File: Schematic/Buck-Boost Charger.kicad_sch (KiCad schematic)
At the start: 79 parts, among them U13 BQ25756RRVR

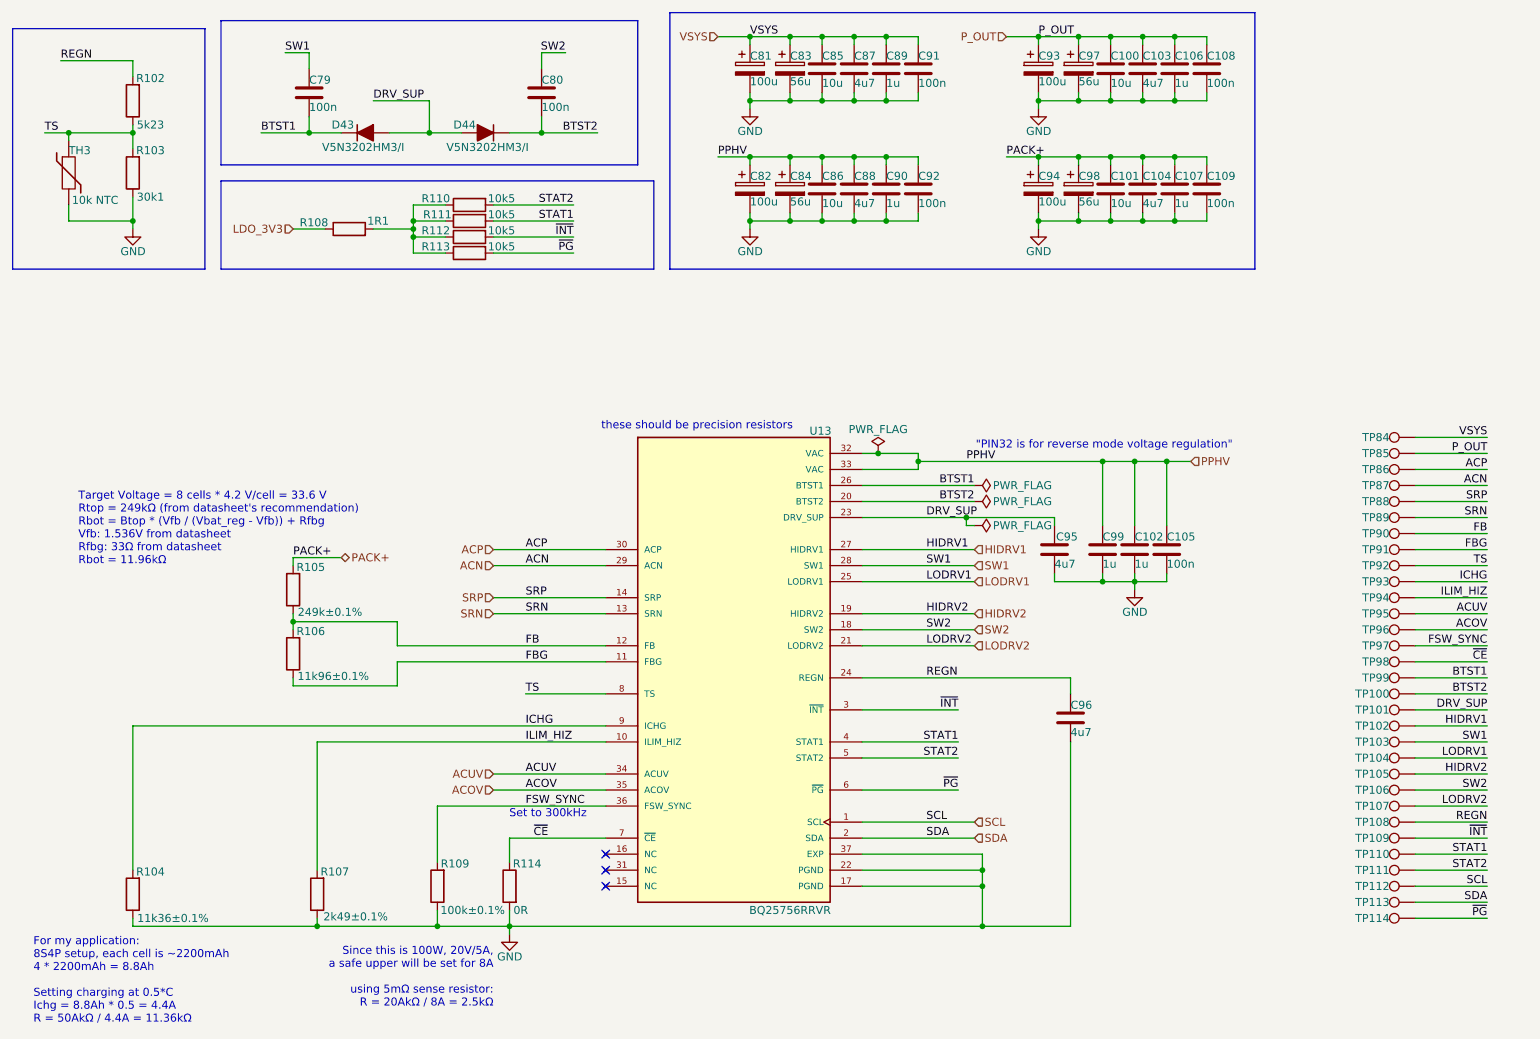
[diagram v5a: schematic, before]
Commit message: updated fuel guage
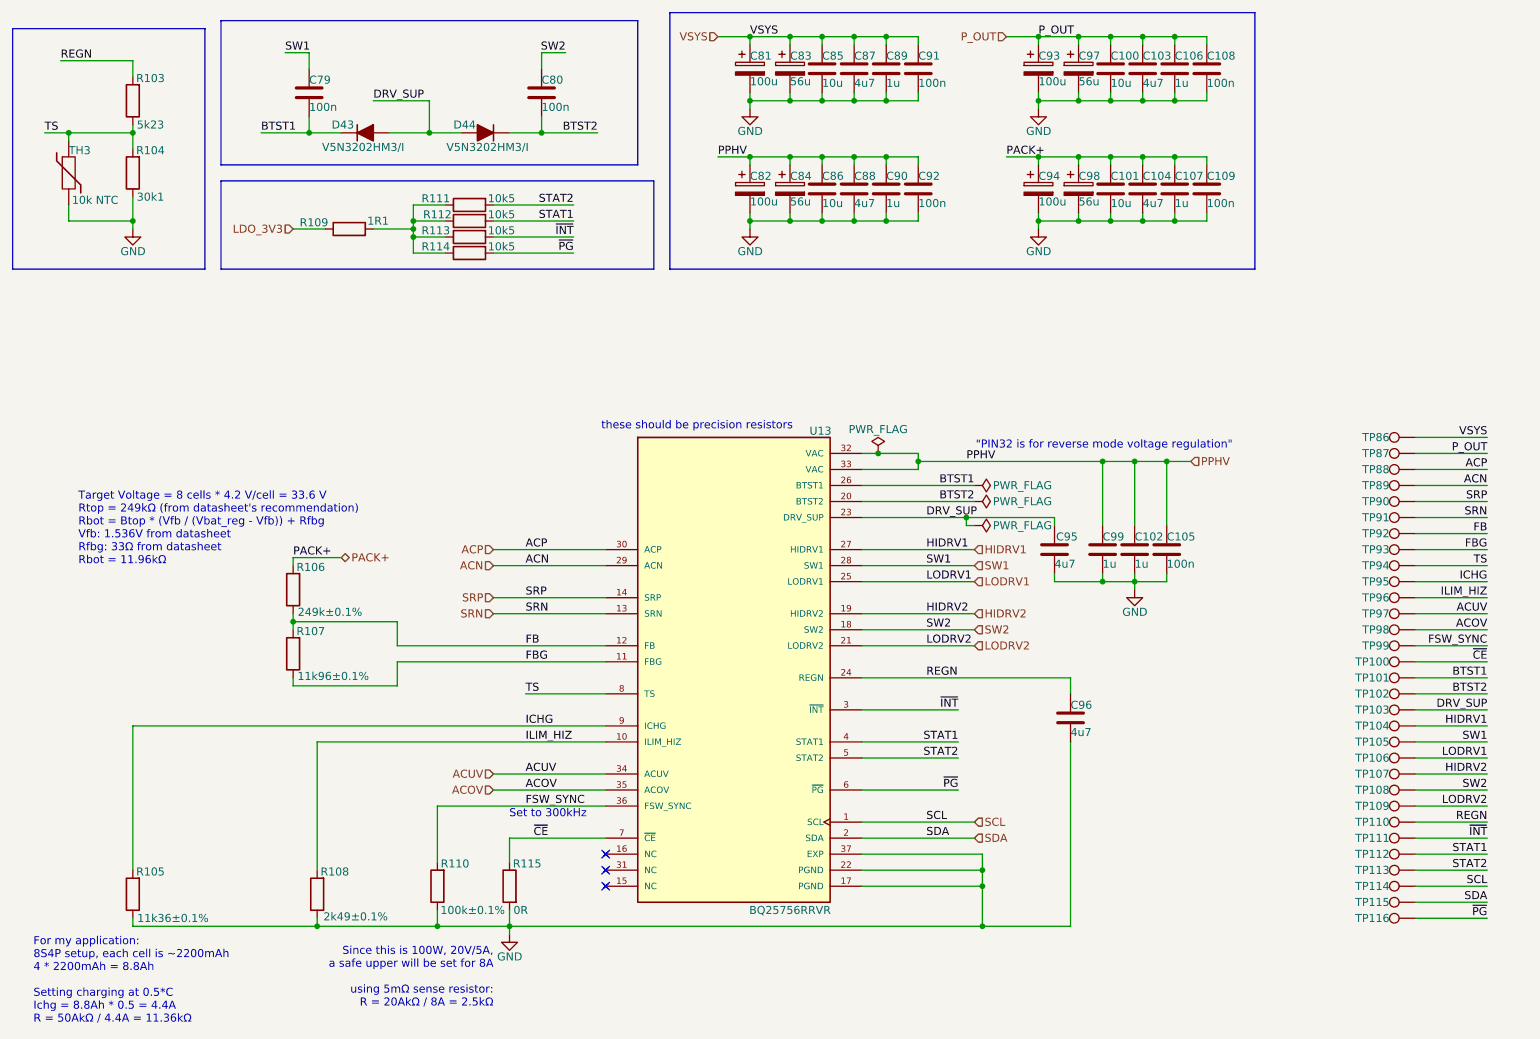
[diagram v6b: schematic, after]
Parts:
- renumbered R102 to R103, R103 to R104, R104 to R105, R105 to R106, R106 to R107, R107 to R108, R108 to R109, R109 to R110, R110 to R111, R111 to R112, R112 to R113, R113 to R114, R114 to R115, TP98 to TP100, TP99 to TP101, TP100 to TP102, TP101 to TP103, TP102 to TP104, TP103 to TP105, TP104 to TP106, TP105 to TP107, TP106 to TP108, TP107 to TP109, TP108 to TP110, TP109 to TP111, TP110 to TP112, TP111 to TP113, TP112 to TP114, TP113 to TP115, TP114 to TP116, TP84 to TP86, TP85 to TP87, TP86 to TP88, TP87 to TP89, TP88 to TP90, TP89 to TP91, TP90 to TP92, TP91 to TP93, TP92 to TP94, TP93 to TP95, TP94 to TP96, TP95 to TP97, TP96 to TP98, TP97 to TP99

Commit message: Added MCU
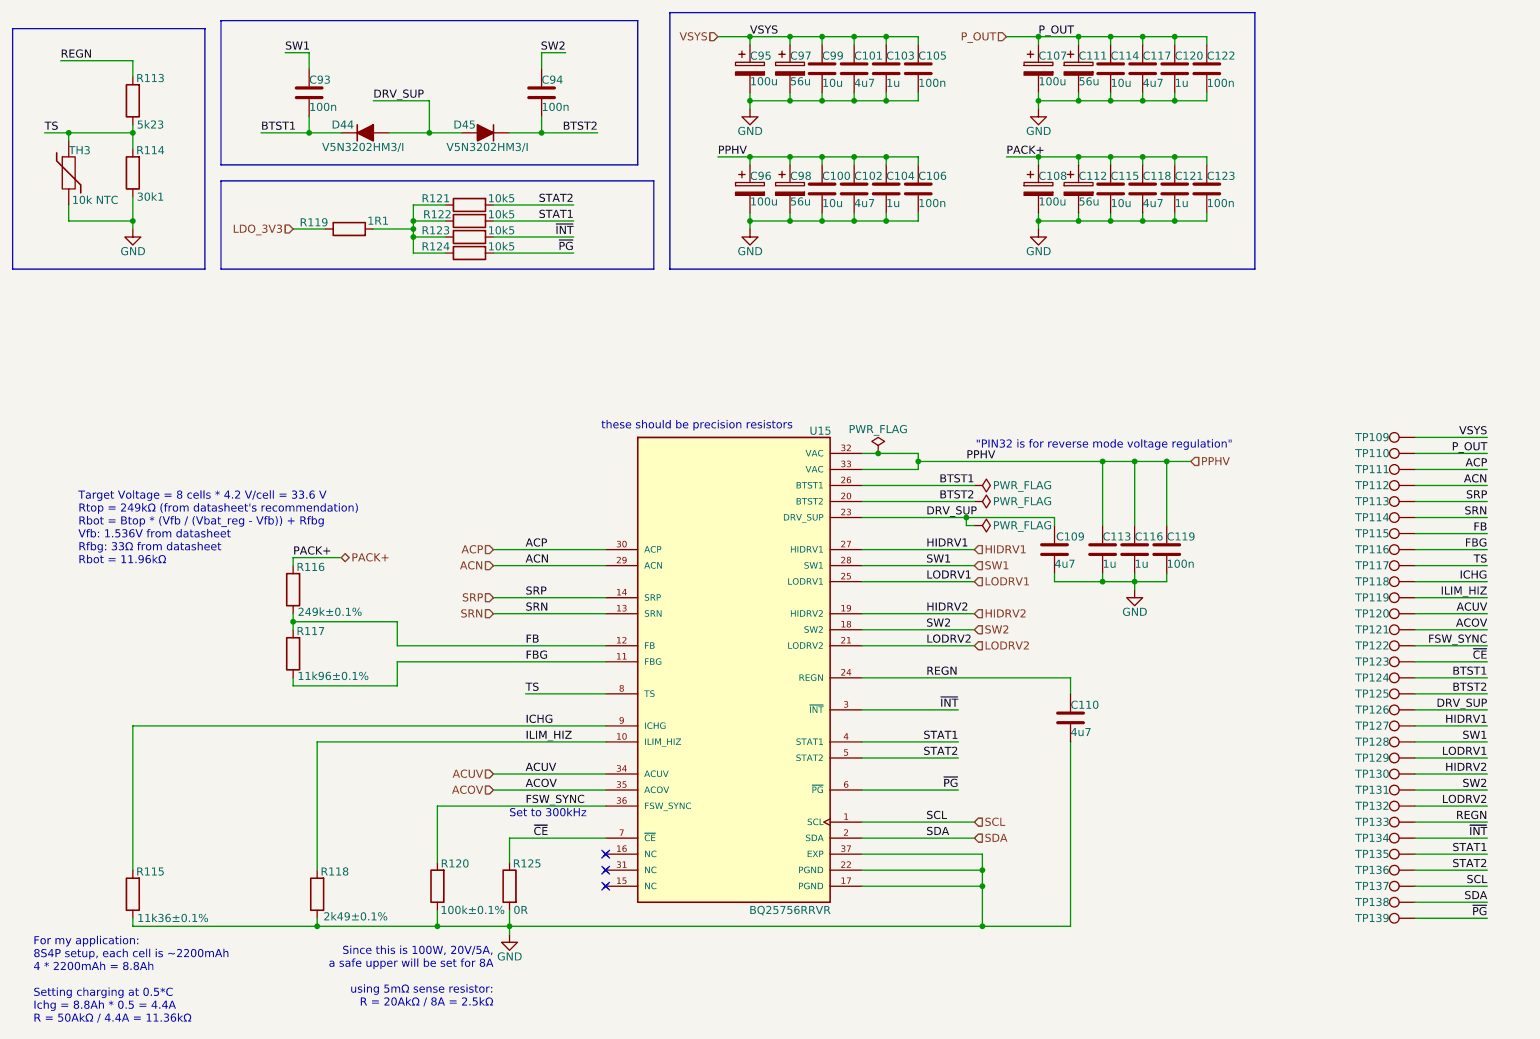
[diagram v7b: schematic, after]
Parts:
- renumbered C86 to C100, C87 to C101, C88 to C102, C89 to C103, C90 to C104, C91 to C105, C92 to C106, C93 to C107, C94 to C108, C95 to C109, C96 to C110, C97 to C111, C98 to C112, C99 to C113, C100 to C114, C101 to C115, C102 to C116, C103 to C117, C104 to C118, C105 to C119, C106 to C120, C107 to C121, C108 to C122, C109 to C123, C79 to C93, C80 to C94, C81 to C95, C82 to C96, C83 to C97, C84 to C98, C85 to C99, D43 to D44, D44 to D45, R103 to R113, R104 to R114, R105 to R115, R106 to R116, R107 to R117, R108 to R118, R109 to R119, R110 to R120, R111 to R121, R112 to R122, R113 to R123, R114 to R124, R115 to R125, TP86 to TP109, TP87 to TP110, TP88 to TP111, TP89 to TP112, TP90 to TP113, TP91 to TP114, TP92 to TP115, TP93 to TP116, TP94 to TP117, TP95 to TP118, TP96 to TP119, TP97 to TP120, TP98 to TP121, TP99 to TP122, TP100 to TP123, TP101 to TP124, TP102 to TP125, TP103 to TP126, TP104 to TP127, TP105 to TP128, TP106 to TP129, TP107 to TP130, TP108 to TP131, TP109 to TP132, TP110 to TP133, TP111 to TP134, TP112 to TP135, TP113 to TP136, TP114 to TP137, TP115 to TP138, TP116 to TP139, U13 to U15

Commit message: Started to work on the BOM
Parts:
- removed C100, C114: 10u, symbol Device:C
- removed C101: 4u7, symbol Device:C
- removed C104, C120: 1u, symbol Device:C
- removed C107, C108, C96: 100u, symbol Device:C_Polarized
- removed C122: 100n, symbol Device:C
- removed C97, C98: 56u, symbol Device:C_Polarized
- removed D44, D45: V5N3202HM3/I, symbol Device:D_Filled
- added C109, C110, C112, C113, C90, C91, C92, C93, C94: 56u, AHA0810560M040R:CAPAE830X1100M, symbol Device:C_Polarized
- added C115, C96, C97: 10u, Capacitor_SMD:C_1206_3216Metric_Pad1.33x1.80mm_HandSolder, symbol Device:C
- added C119: 1u, Capacitor_SMD:C_1206_3216Metric_Pad1.33x1.80mm_HandSolder, symbol Device:C
- added C121: 100n, Capacitor_SMD:C_1206_3216Metric_Pad1.33x1.80mm_HandSolder, symbol Device:C
- added C98: 4u7, Capacitor_SMD:C_1206_3216Metric_Pad1.33x1.80mm_HandSolder, symbol Device:C
- added D41, D42: V5N3202HM3/I, V5N3202HM3-I:DFN33A_VIS, symbol V5N3202HM3-I:V5N3202HM3_I
- C100: renamed from C109; footprint (none) -> Capacitor_SMD:C_1206_3216Metric_Pad1.33x1.80mm_HandSolder; Link (none) -> https://mou.sr/45jYGQI; Manufacturer Part Number (none) -> CL31B475KBHNFNE; Price per Unit (none) -> 0.27; Supplier (none) -> Mouser; Supplier Part Number (none) -> 187-CL31B475KBHNFNE
- C101: renamed from C110; footprint (none) -> Capacitor_SMD:C_1206_3216Metric_Pad1.33x1.80mm_HandSolder; Link (none) -> https://mou.sr/45jYGQI; Manufacturer Part Number (none) -> CL31B475KBHNFNE; Price per Unit (none) -> 0.27; Supplier (none) -> Mouser; Supplier Part Number (none) -> 187-CL31B475KBHNFNE
- C102: value 4u7 -> 1u; footprint (none) -> Capacitor_SMD:C_1206_3216Metric_Pad1.33x1.80mm_HandSolder; Link (none) -> https://mou.sr/41y0aEA; Manufacturer Part Number (none) -> CL31B105KBHNNNE; Price per Unit (none) -> 0.11; Supplier (none) -> Mouser; Supplier Part Number (none) -> 187-CL31B105KBHNNNE
- C103: footprint (none) -> Capacitor_SMD:C_1206_3216Metric_Pad1.33x1.80mm_HandSolder; Link (none) -> https://mou.sr/41y0aEA; Manufacturer Part Number (none) -> CL31B105KBHNNNE; Price per Unit (none) -> 0.11; Supplier (none) -> Mouser; Supplier Part Number (none) -> 187-CL31B105KBHNNNE
- C104: renamed from C113; footprint (none) -> Capacitor_SMD:C_1206_3216Metric_Pad1.33x1.80mm_HandSolder; Link (none) -> https://mou.sr/41y0aEA; Manufacturer Part Number (none) -> CL31B105KBHNNNE; Price per Unit (none) -> 0.11; Supplier (none) -> Mouser; Supplier Part Number (none) -> 187-CL31B105KBHNNNE
- C105, C106: footprint (none) -> Capacitor_SMD:C_1206_3216Metric_Pad1.33x1.80mm_HandSolder; Link (none) -> https://mou.sr/4n9ybmQ; Manufacturer Part Number (none) -> CL31B104KBCNNNC; Price per Unit (none) -> 0.11; Supplier (none) -> Mouser; Supplier Part Number (none) -> 187-CL31B104KBCNNNC
- C107: renamed from C116; footprint (none) -> Capacitor_SMD:C_1206_3216Metric_Pad1.33x1.80mm_HandSolder; Link (none) -> https://mou.sr/41y0aEA; Manufacturer Part Number (none) -> CL31B105KBHNNNE; Price per Unit (none) -> 0.11; Supplier (none) -> Mouser; Supplier Part Number (none) -> 187-CL31B105KBHNNNE
- C108: renamed from C119; footprint (none) -> Capacitor_SMD:C_1206_3216Metric_Pad1.33x1.80mm_HandSolder; Link (none) -> https://mou.sr/4n9ybmQ; Manufacturer Part Number (none) -> CL31B104KBCNNNC; Price per Unit (none) -> 0.11; Supplier (none) -> Mouser; Supplier Part Number (none) -> 187-CL31B104KBCNNNC
- C111: footprint (none) -> AHA0810560M040R:CAPAE830X1100M; Link (none) -> https://mou.sr/4g6lc2W; Manufacturer Part Number (none) -> AHA0810560M040R; Price per Unit (none) -> 1.50; Supplier (none) -> Mouser; Supplier Part Number (none) -> 581-AHA0810560M040R
- C114: renamed from C112; footprint (none) -> AHA0810560M040R:CAPAE830X1100M; Link (none) -> https://mou.sr/4g6lc2W; Manufacturer Part Number (none) -> AHA0810560M040R; Price per Unit (none) -> 1.50; Supplier (none) -> Mouser; Supplier Part Number (none) -> 581-AHA0810560M040R
- C116: renamed from C115; footprint (none) -> Capacitor_SMD:C_1206_3216Metric_Pad1.33x1.80mm_HandSolder; Link (none) -> https://mou.sr/4l54Mdx; Manufacturer Part Number (none) -> CL31A106KBHNNNE; Price per Unit (none) -> 0.11; Supplier (none) -> Mouser; Supplier Part Number (none) -> 187-CL31A106KBHNNNE
- C117, C118: footprint (none) -> Capacitor_SMD:C_1206_3216Metric_Pad1.33x1.80mm_HandSolder; Link (none) -> https://mou.sr/45jYGQI; Manufacturer Part Number (none) -> CL31B475KBHNFNE; Price per Unit (none) -> 0.27; Supplier (none) -> Mouser; Supplier Part Number (none) -> 187-CL31B475KBHNFNE
- C120: renamed from C121; footprint (none) -> Capacitor_SMD:C_1206_3216Metric_Pad1.33x1.80mm_HandSolder; Link (none) -> https://mou.sr/41y0aEA; Manufacturer Part Number (none) -> CL31B105KBHNNNE; Price per Unit (none) -> 0.11; Supplier (none) -> Mouser; Supplier Part Number (none) -> 187-CL31B105KBHNNNE
- C122: renamed from C123; footprint (none) -> Capacitor_SMD:C_1206_3216Metric_Pad1.33x1.80mm_HandSolder; Link (none) -> https://mou.sr/4n9ybmQ; Manufacturer Part Number (none) -> CL31B104KBCNNNC; Price per Unit (none) -> 0.11; Supplier (none) -> Mouser; Supplier Part Number (none) -> 187-CL31B104KBCNNNC
- C88: renamed from C93; footprint (none) -> Capacitor_SMD:C_1206_3216Metric_Pad1.33x1.80mm_HandSolder; Link (none) -> https://mou.sr/4n9ybmQ; Manufacturer Part Number (none) -> CL31B104KBCNNNC; Price per Unit (none) -> 0.11; Supplier (none) -> Mouser; Supplier Part Number (none) -> 187-CL31B104KBCNNNC
- C89: renamed from C94; footprint (none) -> Capacitor_SMD:C_1206_3216Metric_Pad1.33x1.80mm_HandSolder; Link (none) -> https://mou.sr/4n9ybmQ; Manufacturer Part Number (none) -> CL31B104KBCNNNC; Price per Unit (none) -> 0.11; Supplier (none) -> Mouser; Supplier Part Number (none) -> 187-CL31B104KBCNNNC
- C95: value 100u -> 56u; footprint (none) -> AHA0810560M040R:CAPAE830X1100M; Link (none) -> https://mou.sr/4g6lc2W; Manufacturer Part Number (none) -> AHA0810560M040R; Price per Unit (none) -> 1.50; Supplier (none) -> Mouser; Supplier Part Number (none) -> 581-AHA0810560M040R
- C99: value 10u -> 4u7; footprint (none) -> Capacitor_SMD:C_1206_3216Metric_Pad1.33x1.80mm_HandSolder; Link (none) -> https://mou.sr/45jYGQI; Manufacturer Part Number (none) -> CL31B475KBHNFNE; Price per Unit (none) -> 0.27; Supplier (none) -> Mouser; Supplier Part Number (none) -> 187-CL31B475KBHNFNE
- U13: renamed from U15; footprint BQ25756RRVR:IC_BQ25756RRVR -> (none); Price None -> (none)
- renumbered R113 to R109, R114 to R110, R115 to R111, R119 to R112, R116 to R113, R117 to R114, R121 to R115, R122 to R116, R123 to R117, R124 to R118, R118 to R119, R125 to R121, TP123 to TP100, TP124 to TP101, TP125 to TP102, TP126 to TP103, TP127 to TP104, TP128 to TP105, TP129 to TP106, TP130 to TP107, TP131 to TP108, TP132 to TP109, TP133 to TP110, TP134 to TP111, TP135 to TP112, TP136 to TP113, TP137 to TP114, TP138 to TP115, TP139 to TP116, TP109 to TP86, TP110 to TP87, TP111 to TP88, TP112 to TP89, TP113 to TP90, TP114 to TP91, TP115 to TP92, TP116 to TP93, TP117 to TP94, TP118 to TP95, TP119 to TP96, TP120 to TP97, TP121 to TP98, TP122 to TP99
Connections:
- net BTST1: now also D42.5, D42.6, D42.7, D42.8
- net BTST2: now also D41.5, D41.6, D41.7, D41.8
- net DRV_SUP: now also D41.1, D41.2, D41.3, D41.4, D42.1, D42.2, D42.3, D42.4
- net GND: now also C109.2, C110.2, C112.2, C113.2, C115.2, C119.2, C121.2, C90.2, C91.2, C92.2, C93.2, C94.2, C96.2, C97.2, C98.2
- net PACK+: now also C110.1, C112.1
- net PPHV: now also C111.1, C117.1, C109.1, C113.1, C115.1, C119.1, C121.1; no longer C102.1, C106.1
- net P_OUT: now also C103.1, C106.1, C95.1, C99.1, C91.1, C93.1, C97.1; no longer C111.1, C117.1
- net VSYS: now also C102.1, C90.1, C92.1, C94.1, C96.1, C98.1; no longer C103.1, C95.1, C99.1
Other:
- moved on the sheet: C107, C108, C114, C116, C118, C120, C122, C89, R112, R115, R116, R117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
